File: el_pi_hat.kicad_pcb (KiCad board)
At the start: 2 copper layers, 65 x 56 mm, 80 parts, among them J1 12V, J2 UART, J3 Raspberry Pi Header, J4 TRX, J5 MIC, J6 LINE OUT, J7 LINE IN, J8 HP OUT, Q1 2N7002, Q2 2N7002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

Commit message: Dropping 3M32 resistor to 1M4.
The DC/DC converter is currently trimmed to 5.1 V. Since the
Raspberry Pi can take more than that, we increase the voltage
to 5.25 V. This appears to be the recommended operating voltage.

In order to achieve this, a trimming resistor of 1M375 is
required. We use 1M4. Since we also use this resistor value to
dissipate stray charge on FET and microcontroller inputs, those
resistors are dropped in value as well. This is a good thing since
the value was uncomfortably high (and still remains somewhat high
even after the change).

Fixes #2.
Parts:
- R1, R14, R18, R29, R3: value 3M32 -> 1M4

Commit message: Adding diode to address case where DC/DC converter is reverse biased
The datasheet of the DC/DC converter recommends a (normally) reverse
biased diode across the regulator. This is to prevent damage in case
the output is at a higher voltage than the input.

Since this condition would apply if somebody powers the Raspberry Pi
directly (i.e. not using the hat), it is strongly recommended to add
the diode.

Fixes #1
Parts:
- added D5: B340, Diode_SMD:D_SMC, F.Cu at (50.8, 37.8)
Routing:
- net +12V: track 12.8 -> 23.9 mm
- net GND: vias 251 -> 248
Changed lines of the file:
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@@
     (thickness 1.6)
     (drawings 52)
-    (tracks 631)
+    (tracks 633)
     (zones 0)
-    (modules 80)
+    (modules 81)
     (nets 81)
   )
@@
   )
   (setup
-    (last_trace_width 0.25)
+    (last_trace_width 1)
     (user_trace_width 0.15)
     (user_trace_width 0.25)
@@
     (add_net "Net-(Y1-Pad4)")
   )
+  (module Diode_SMD:D_SMC (layer F.Cu)
+    (at 50.75 37.75 90)
+    (descr "Diode SMC (DO-214AB)")
+    (tags "Diode SMC (DO-214AB)")
+    (attr smd)
+    (fp_text reference D5 (at 2.5 5 180) (layer F.SilkS)
+      (effects (font (size 0.75 0.75) (thickness 0.12)))
+    )
+    (fp_text value B340 (at 0 4.2 90) (layer F.Fab)
+      (effects (font (size 1 1) (thickness 0.15)))
+    )
+    (fp_text user %R (at 0 -1.9 90) (layer F.Fab)
+      (effects (font (size 1 1) (thickness 0.15)))
+    )
+    (fp_line (start -4.8 3.25) (end -4.8 -3.25) (layer F.SilkS) (width 0.12))
+    (fp_line (start 3.55 3.1) (end -3.55 3.1) (layer F.Fab) (width 0.1))
+    (fp_line (start -3.55 3.1) (end -3.55 -3.1) (layer F.Fab) (width 0.1))
+    (fp_line (start 3.55 -3.1) (end 3.55 3.1) (layer F.Fab) (width 0.1))
+    (fp_line (start 3.55 -3.1) (end -3.55 -3.1) (layer F.Fab) (width 0.1))
+    (fp_line (start -4.9 -3.35) (end 4.9 -3.35) (layer F.CrtYd) (width 0.05))
+    (fp_line (start 4.9 -3.35) (end 4.9 3.35) (layer F.CrtYd) (width 0.05))
+    (fp_line (start 4.9 3.35) (end -4.9 3.35) (layer F.CrtYd) (width 0.05))
+    (fp_line (start -4.9 3.35) (end -4.9 -3.35) (layer F.CrtYd) (width 0.05))
+    (fp_line (start -0.64944 0.00102) (end -1.55114 0.00102) (layer F.Fab) (width 0.1))
+    (fp_line (start 0.50118 0.00102) (end 1.4994 0.00102) (layer F.Fab) (width 0.1))
+    (fp_line (start -0.64944 -0.79908) (end -0.64944 0.80112) (layer F.Fab) (width 0.1))
+    (fp_line (start 0.50118 0.75032) (end 0.50118 -0.79908) (layer F.Fab) (width 0.1))
+    (fp_line (start -0.64944 0.00102) (end 0.50118 0.75032) (layer F.Fab) (width 0.1))
+    (fp_line (start -0.64944 0.00102) (end 0.50118 -0.79908) (layer F.Fab) (width 0.1))
+    (fp_line (start -4.8 3.25) (end 3.6 3.25) (layer F.SilkS) (width 0.12))
+    (fp_line (start -4.8 -3.25) (end 3.6 -3.25) (layer F.SilkS) (width 0.12))
+    (pad 2 smd rect (at 3.4 0 180) (size 3.3 2.5) (layers F.Cu F.Paste F.Mask)
+      (net 35 +5V))
+    (pad 1 smd rect (at -3.4 0 180) (size 3.3 2.5) (layers F.Cu F.Paste F.Mask)
+      (net 5 +12V))
+    (model ${KISYS3DMOD}/Diode_SMD.3dshapes/D_SMC.wrl
+      (at (xyz 0 0 0))
+      (scale (xyz 1 1 1))
+      (rotate (xyz 0 0 0))
+    )
+  )
   (module Crystal:Crystal_SMD_3225-4Pin_3.2x2.5mm (layer F.Cu)
     (at 107.5 48.25 270)
@@
   (via (at 50 44) (size 0.6) (drill 0.4) (layers F.Cu B.Cu) (net 3))
   (via (at 52 44) (size 0.6) (drill 0.4) (layers F.Cu B.Cu) (net 3))
-  (via (at 54 44) (size 0.6) (drill 0.4) (layers F.Cu B.Cu) (net 3))
   (via (at 53 46) (size 0.6) (drill 0.4) (layers F.Cu B.Cu) (net 3))
-  (via (at 55 46) (size 0.6) (drill 0.4) (layers F.Cu B.Cu) (net 3))
-  (via (at 55 48) (size 0.6) (drill 0.4) (layers F.Cu B.Cu) (net 3))
   (via (at 53 48) (size 0.6) (drill 0.4) (layers F.Cu B.Cu) (net 3))
   (via (at 55 50) (size 0.6) (drill 0.4) (layers F.Cu B.Cu) (net 3))
@@
   (segment (start 60 54.375) (end 60 53.5) (width 1) (layer F.Cu) (net 5))
   (segment (start 59 52.5) (end 56.75 52.5) (width 1) (layer F.Cu) (net 5))
+  (segment (start 50.75 41.15) (end 52.4 41.15) (width 1) (layer F.Cu) (net 5))
+  (segment (start 52.4 41.15) (end 54.5 43.25) (width 1) (layer F.Cu) (net 5))
+  (segment (start 54.5 43.25) (end 54.5 47) (width 1) (layer F.Cu) (net 5))
+  (segment (start 55.79 48.29) (end 56.67 48.29) (width 1) (layer F.Cu) (net 5))
+  (segment (start 54.5 47) (end 55.79 48.29) (width 1) (layer F.Cu) (net 5))
   (segment (start 71 43.75) (end 72.5 43.75) (width 0.5) (layer F.Cu) (net 6))
   (segment (start 72.75 43.5) (end 72.75 42.65) (width 0.5) (layer F.Cu) (net 6))

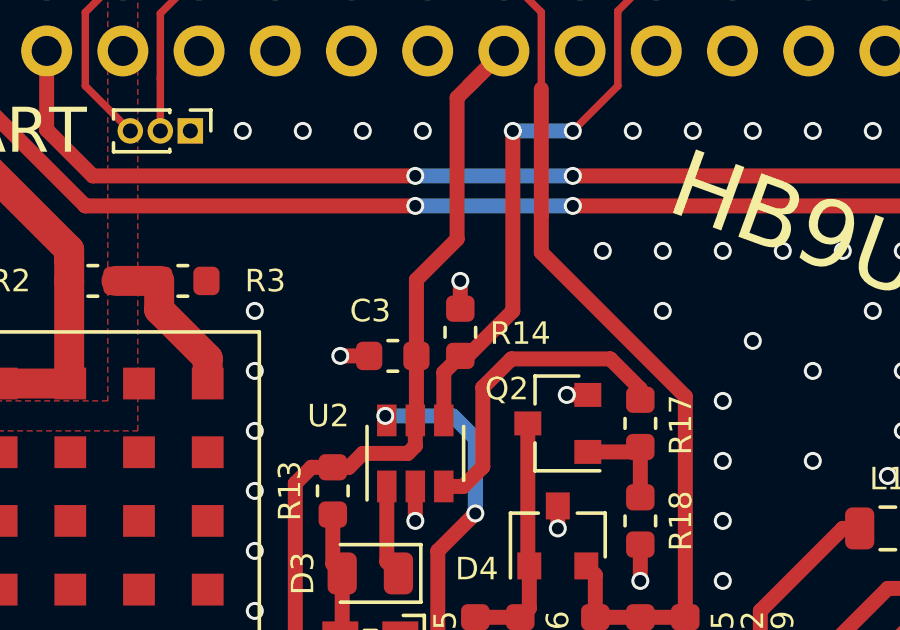
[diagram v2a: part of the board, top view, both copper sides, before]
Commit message: Adding ability to short out ATtiny chip
In case somebody decides not to use the Quaselsperre PTT timeout
timer watchdog, it would be nice to have a normally unpopulated
resistor that would connect the PTT input to the PTT output.

The documentation was updated accordingly.

Fixes #3.
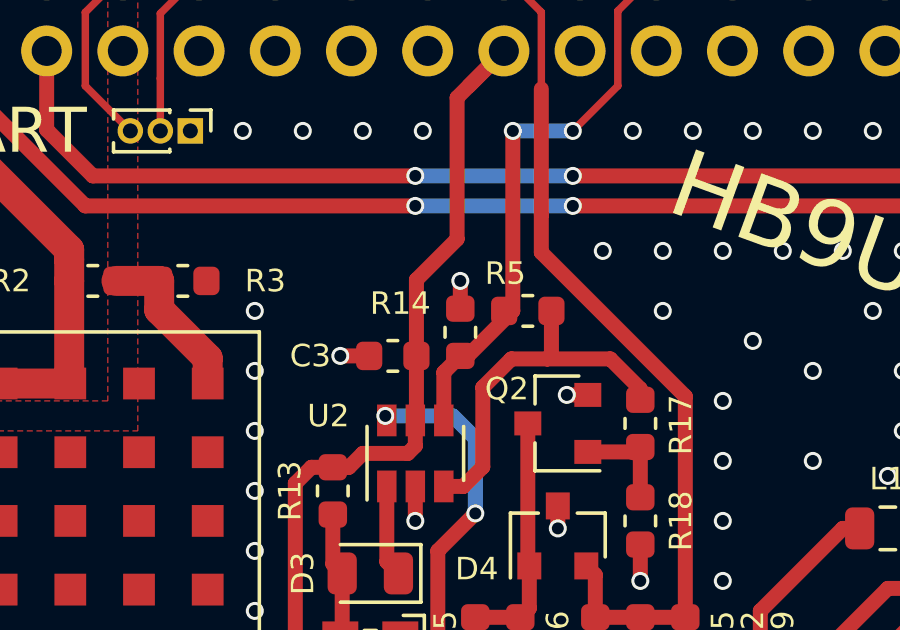
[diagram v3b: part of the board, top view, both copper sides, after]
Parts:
- added R5: NP, Resistor_SMD:R_0603_1608Metric, F.Cu at (76.5, 39.0)
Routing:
- net Net-(R17-Pad2): track 10.6 -> 12.3 mm
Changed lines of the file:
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@@
     (thickness 1.6)
     (drawings 52)
-    (tracks 633)
+    (tracks 636)
     (zones 0)
-    (modules 81)
+    (modules 82)
     (nets 81)
   )
@@
   )
   (setup
-    (last_trace_width 1)
+    (last_trace_width 0.5)
     (user_trace_width 0.15)
     (user_trace_width 0.25)
@@
     (add_net "Net-(Y1-Pad4)")
   )
+  (module Resistor_SMD:R_0603_1608Metric (layer F.Cu)
+    (at 76.5 39 180)
+    (descr "Resistor SMD 0603 (1608 Metric), square (rectangular) end terminal, IPC_7351 nominal, (Body size source: http://www.tortai-tech.com/upload/download/2011102023233369053.pdf), generated with kicad-footprint-generator")
+    (tags resistor)
+    (attr smd)
+    (fp_text reference R5 (at 0.75 1.25) (layer F.SilkS)
+      (effects (font (size 0.75 0.75) (thickness 0.12)))
+    )
+    (fp_text value NP (at 0 1.43) (layer F.Fab)
+      (effects (font (size 1 1) (thickness 0.15)))
+    )
+    (fp_text user %R (at 0 0) (layer F.Fab)
+      (effects (font (size 0.4 0.4) (thickness 0.06)))
+    )
+    (fp_line (start -0.8 0.4) (end -0.8 -0.4) (layer F.Fab) (width 0.1))
+    (fp_line (start -0.8 -0.4) (end 0.8 -0.4) (layer F.Fab) (width 0.1))
+    (fp_line (start 0.8 -0.4) (end 0.8 0.4) (layer F.Fab) (width 0.1))
+    (fp_line (start 0.8 0.4) (end -0.8 0.4) (layer F.Fab) (width 0.1))
+    (fp_line (start -0.162779 -0.51) (end 0.162779 -0.51) (layer F.SilkS) (width 0.12))
+    (fp_line (start -0.162779 0.51) (end 0.162779 0.51) (layer F.SilkS) (width 0.12))
+    (fp_line (start -1.48 0.73) (end -1.48 -0.73) (layer F.CrtYd) (width 0.05))
+    (fp_line (start -1.48 -0.73) (end 1.48 -0.73) (layer F.CrtYd) (width 0.05))
+    (fp_line (start 1.48 -0.73) (end 1.48 0.73) (layer F.CrtYd) (width 0.05))
+    (fp_line (start 1.48 0.73) (end -1.48 0.73) (layer F.CrtYd) (width 0.05))
+    (pad 2 smd roundrect (at 0.7875 0 180) (size 0.875 0.95) (layers F.Cu F.Paste F.Mask) (roundrect_rratio 0.25)
+      (net 48 /PI_PTT))
+    (pad 1 smd roundrect (at -0.7875 0 180) (size 0.875 0.95) (layers F.Cu F.Paste F.Mask) (roundrect_rratio 0.25)
+      (net 49 "Net-(R17-Pad2)"))
+    (model ${KISYS3DMOD}/Resistor_SMD.3dshapes/R_0603_1608Metric.wrl
+      (at (xyz 0 0 0))
+      (scale (xyz 1 1 1))
+      (rotate (xyz 0 0 0))
+    )
+  )
   (module Diode_SMD:D_SMC (layer F.Cu)
     (at 50.75 37.75 90)
@@
     (tags resistor)
     (attr smd)
-    (fp_text reference R14 (at -0.0375 2 180) (layer F.SilkS)
+    (fp_text reference R14 (at 0.9625 -2 180) (layer F.SilkS)
       (effects (font (size 0.75 0.75) (thickness 0.12)))
     )
@@
     (tags capacitor)
     (attr smd)
-    (fp_text reference C3 (at 0.75 1.5) (layer F.SilkS)
+    (fp_text reference C3 (at 2.75 0) (layer F.SilkS)
       (effects (font (size 0.75 0.75) (thickness 0.12)))
     )
@@
   (segment (start 73.7 42.65) (end 73.7 41.05) (width 0.5) (layer F.Cu) (net 48))
   (segment (start 74.25 40.5) (end 74.5 40.5) (width 0.5) (layer F.Cu) (net 48))
-  (segment (start 74.5 40.5) (end 76 39) (width 0.5) (layer F.Cu) (net 48))
   (segment (start 76 39) (end 76 33) (width 0.5) (layer F.Cu) (net 48))
   (via (at 76 33) (size 0.6) (drill 0.4) (layers F.Cu B.Cu) (net 48))
@@
   (segment (start 79.5 31.5) (end 78 33) (width 0.25) (layer F.Cu) (net 48))
   (segment (start 79.5 29) (end 79.5 31.5) (width 0.25) (layer F.Cu) (net 48))
+  (segment (start 74.5 40.5) (end 76 39) (width 0.5) (layer F.Cu) (net 48))
   (segment (start 80.25 41.9625) (end 80.25 41.6) (width 0.5) (layer F.Cu) (net 49))
   (segment (start 80.25 41.6) (end 79.25 40.6) (width 0.5) (layer F.Cu) (net 49))
-  (segment (start 79.25 40.6) (end 75.95 40.6) (width 0.5) (layer F.Cu) (net 49))
   (segment (start 75.95 40.6) (end 75 41.55) (width 0.5) (layer F.Cu) (net 49))
   (segment (start 75 41.55) (end 75 44.2) (width 0.5) (layer F.Cu) (net 49))
   (segment (start 74.35 44.85) (end 73.7 44.85) (width 0.5) (layer F.Cu) (net 49))
   (segment (start 75 44.2) (end 74.35 44.85) (width 0.5) (layer F.Cu) (net 49))
+  (segment (start 77.2875 40.4625) (end 77.15 40.6) (width 0.5) (layer F.Cu) (net 49))
+  (segment (start 77.2875 39) (end 77.2875 40.4625) (width 0.5) (layer F.Cu) (net 49))
+  (segment (start 77.15 40.6) (end 75.95 40.6) (width 0.5) (layer F.Cu) (net 49))
+  (segment (start 79.25 40.6) (end 77.15 40.6) (width 0.5) (layer F.Cu) (net 49))
   (via (at 71.75 42.5) (size 0.6) (drill 0.4) (layers F.Cu B.Cu) (net 53))
   (segment (start 71.8 42.55) (end 71.75 42.5) (width 0.5) (layer F.Cu) (net 53))

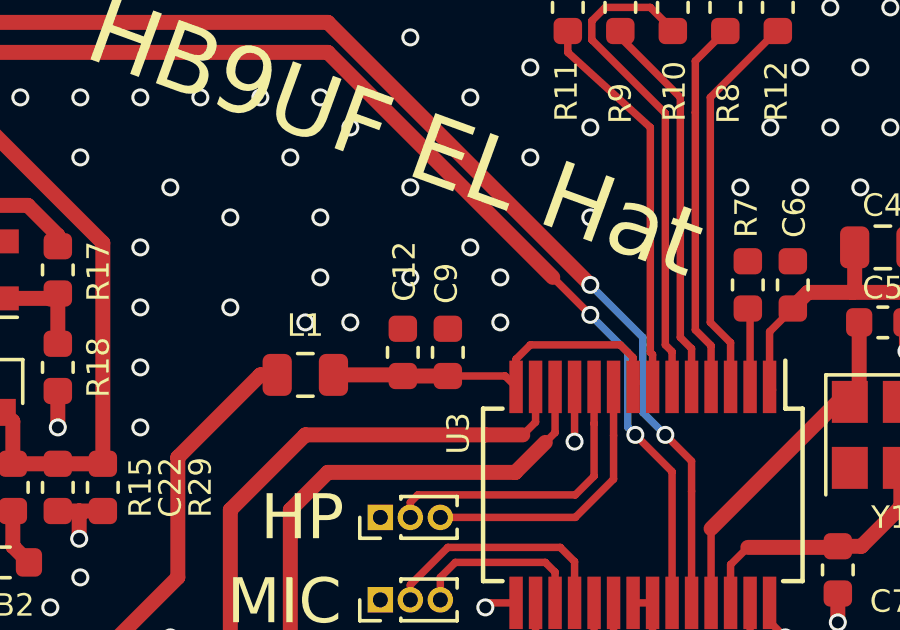
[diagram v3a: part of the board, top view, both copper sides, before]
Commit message: Relocating decoupling capacitor for HPVDD.
The capacitor was misplaced, leading to poor decoupling. While we
never observed issues in this regard with Rev 1.0, this is still
a good opportunity to address this.

Fixes #5.
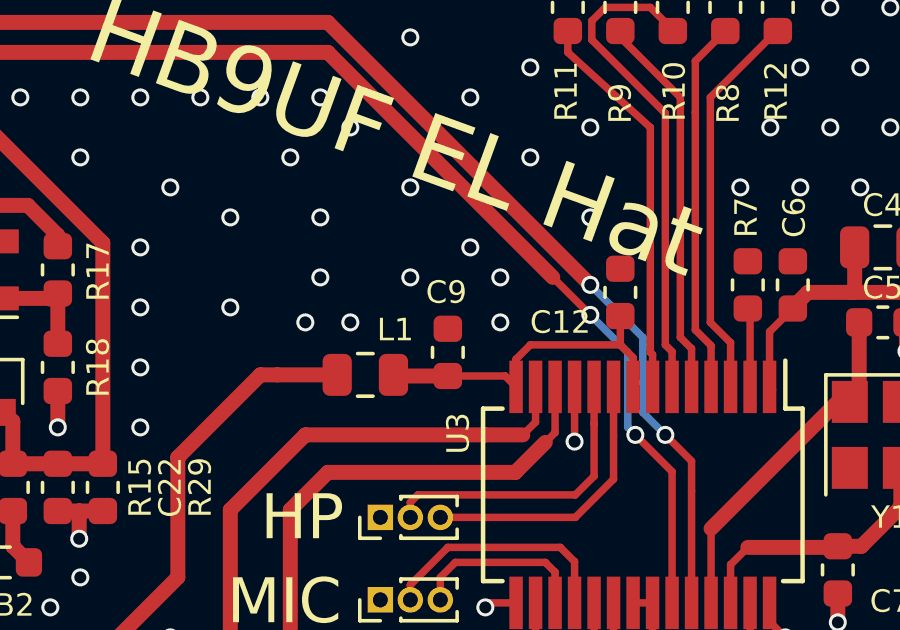
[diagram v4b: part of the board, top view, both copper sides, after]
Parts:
- moved C12 7.52 mm to (99.0, 43.5)
- moved L1 2.00 mm to (90.5, 46.2)
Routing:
- net +3V3: track 153.2 -> 155.2 mm
- net Net-(C12-Pad1): track 12.4 -> 11.1 mm
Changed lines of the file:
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@@
     (thickness 1.6)
     (drawings 52)
-    (tracks 636)
+    (tracks 637)
     (zones 0)
     (modules 82)
@@
   )
   (setup
-    (last_trace_width 0.5)
+    (last_trace_width 0.25)
     (user_trace_width 0.15)
     (user_trace_width 0.25)
@@
   )
   (module Inductor_SMD:L_0805_2012Metric (layer F.Cu)
-    (at 88.5 46.25)
+    (at 90.5 46.25)
     (descr "Inductor SMD 0805 (2012 Metric), square (rectangular) end terminal, IPC_7351 nominal, (Body size source: https://docs.google.com/spreadsheets/d/1BsfQQcO9C6DZCsRaXUlFlo91Tg2WpOkGARC1WS5S8t0/edit?usp=sharing), generated with kicad-footprint-generator")
     (tags inductor)
     (attr smd)
-    (fp_text reference L1 (at 0 -1.65) (layer F.SilkS)
+    (fp_text reference L1 (at 1 -1.5) (layer F.SilkS)
       (effects (font (size 0.75 0.75) (thickness 0.12)))
     )
@@
   )
   (module Capacitor_SMD:C_0603_1608Metric (layer F.Cu)
-    (at 91.75 45.5 90)
+    (at 99 43.5 90)
     (descr "Capacitor SMD 0603 (1608 Metric), square (rectangular) end terminal, IPC_7351 nominal, (Body size source: http://www.tortai-tech.com/upload/download/2011102023233369053.pdf), generated with kicad-footprint-generator")
     (tags capacitor)
     (attr smd)
-    (fp_text reference C12 (at 2.7 0.05 90) (layer F.SilkS)
+    (fp_text reference C12 (at -1 -2 180) (layer F.SilkS)
       (effects (font (size 0.75 0.75) (thickness 0.12)))
     )
@@
     (tags capacitor)
     (attr smd)
-    (fp_text reference C9 (at 2.3 -0.05 90) (layer F.SilkS)
+    (fp_text reference C9 (at 2 -0.05 180) (layer F.SilkS)
       (effects (font (size 0.75 0.75) (thickness 0.12)))
     )
@@
   (segment (start 110.5 53) (end 110.5 44) (width 0.5) (layer F.Cu) (net 6))
   (segment (start 103.9625 55.9625) (end 107.5375 55.9625) (width 0.5) (layer F.Cu) (net 6))
+  (segment (start 87.5625 46.25) (end 89.5625 46.25) (width 0.5) (layer F.Cu) (net 6))
   (segment (start 102.025 53.85) (end 102.025 51.375) (width 0.25) (layer F.Cu) (net 7))
   (segment (start 106.6 46.8) (end 102.025 51.375) (width 0.5) (layer F.Cu) (net 7))
@@
   (segment (start 96 45.25) (end 95.525 45.725) (width 0.25) (layer F.Cu) (net 9))
   (segment (start 91.7125 46.25) (end 91.75 46.2875) (width 0.5) (layer F.Cu) (net 9))
-  (segment (start 89.4375 46.25) (end 91.7125 46.25) (width 0.5) (layer F.Cu) (net 9))
+  (segment (start 99 44.2875) (end 99 45.25) (width 0.25) (layer F.Cu) (net 9))
   (segment (start 92.85 56.8125) (end 93.25 57.2125) (width 0.5) (layer F.Cu) (net 10))
   (segment (start 91.5 56.8125) (end 92.85 56.8125) (width 0.5) (layer F.Cu) (net 10))
